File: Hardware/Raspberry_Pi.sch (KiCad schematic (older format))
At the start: 4 parts, among them J1 M20-9762042

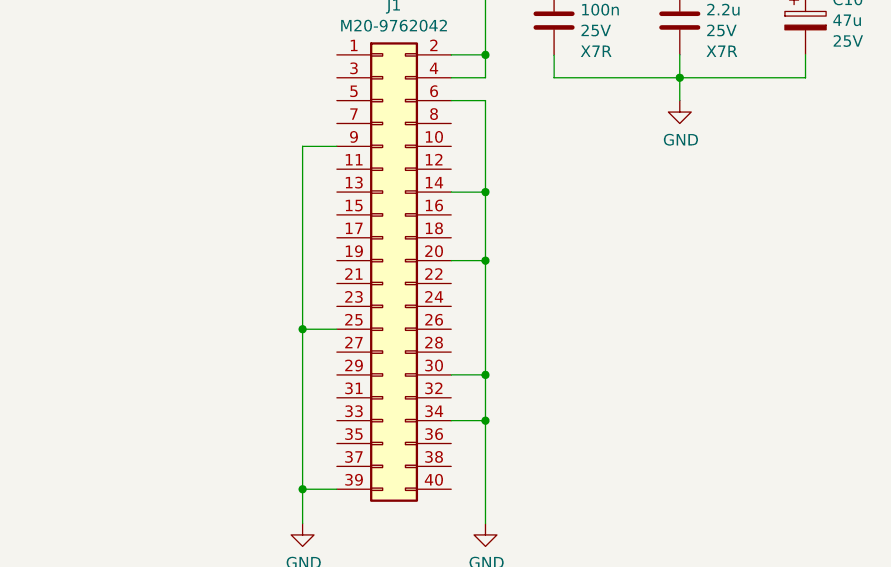
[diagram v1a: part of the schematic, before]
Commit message: [Hardware] Connected ADC to Raspberry Pi through SPI bus.
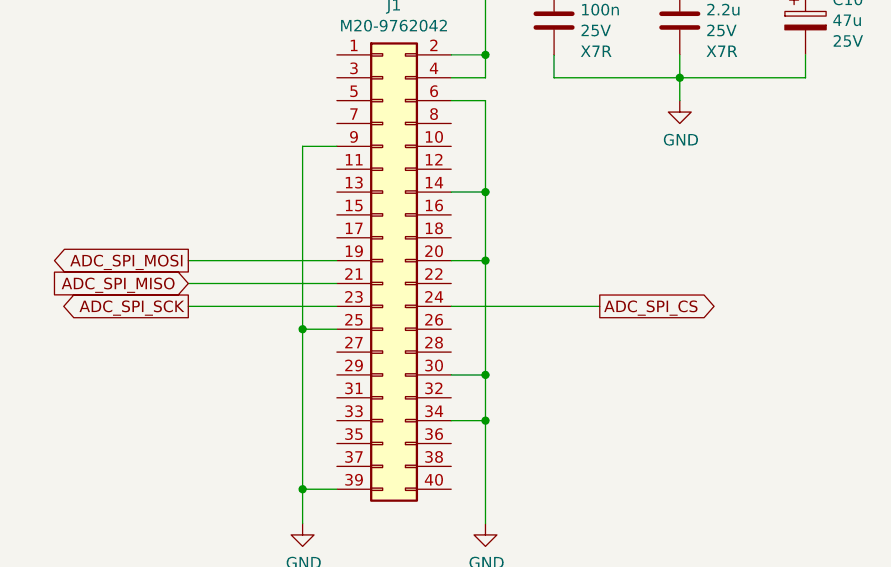
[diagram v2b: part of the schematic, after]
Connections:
- net ADC_SPI_MOSI: now reaches J1.19 (Pin_19)
- net ADC_SPI_MISO: now reaches J1.21 (Pin_21)
- net ADC_SPI_SCK: now reaches J1.23 (Pin_23)
- net ADC_SPI_CS: now reaches J1.24 (Pin_24)
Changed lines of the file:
@@
 Wire Wire Line
 	5050 3950 5050 4100
+Wire Wire Line
+	5200 3150 4550 3150
+Text GLabel 4550 3150 0    50   Output ~ 0
+ADC_SPI_SCK
+Wire Wire Line
+	5200 3050 4550 3050
+Text GLabel 4550 3050 0    50   Input ~ 0
+ADC_SPI_MISO
+Text GLabel 4550 2950 0    50   Output ~ 0
+ADC_SPI_MOSI
+Wire Wire Line
+	5200 2950 4550 2950
+Wire Wire Line
+	6350 3150 5700 3150
+Text GLabel 6350 3150 2    50   Output ~ 0
+ADC_SPI_CS
 $EndSCHEMATC

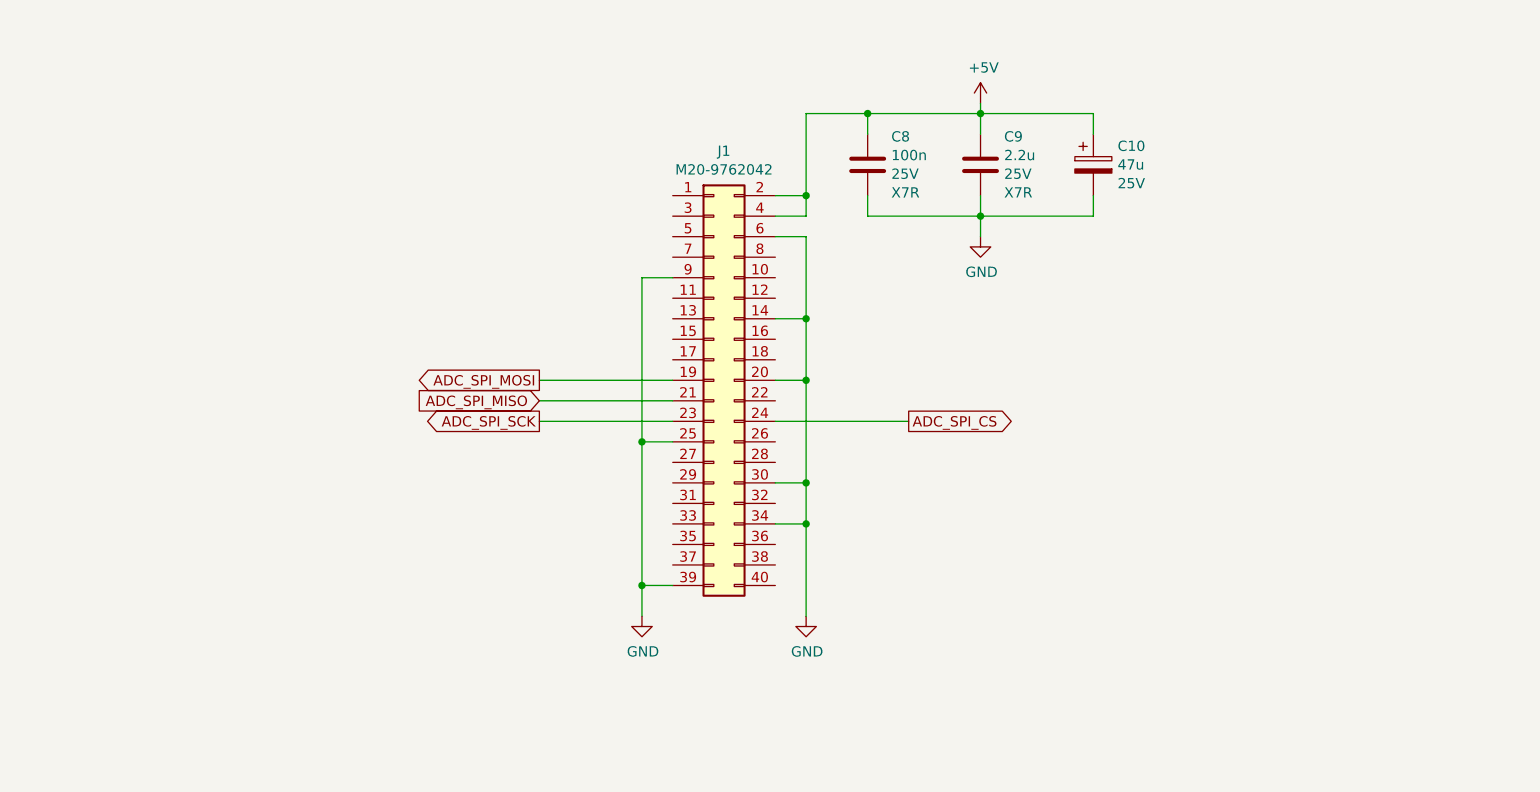
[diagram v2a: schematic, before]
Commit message: [Hardware] Added servomotors supply parts and connected them to Raspberry Pi PWMs.
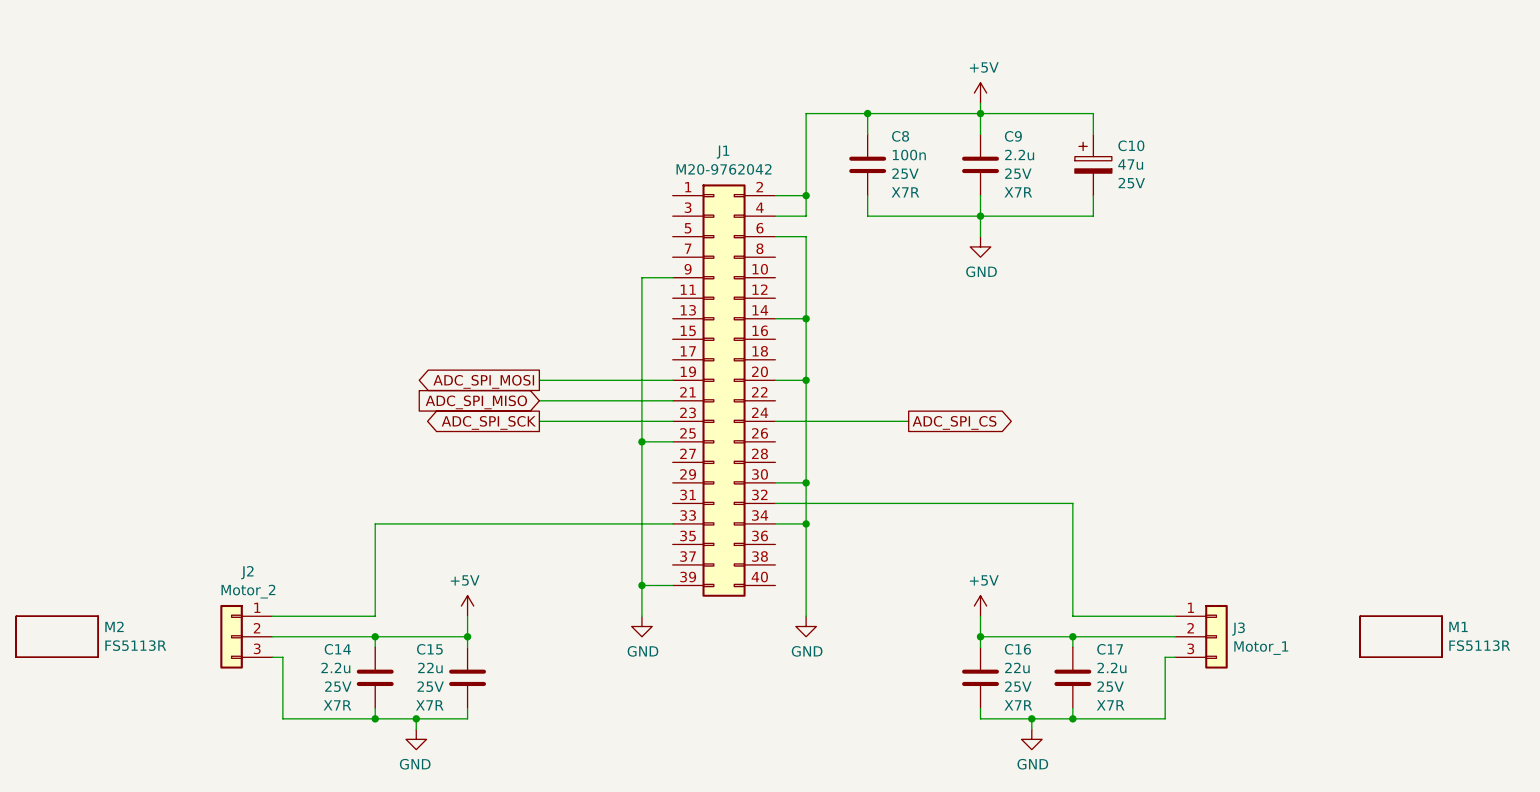
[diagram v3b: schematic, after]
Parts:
- added C14, C17: 2.2u, Capacitor_SMD:C_1206_3216Metric_Pad1.42x1.75mm_HandSolder, symbol Device:C
- added C15, C16: 22u, Capacitor_SMD:C_1206_3216Metric_Pad1.42x1.75mm_HandSolder, symbol Device:C
- added J2: Motor_2, Connector_PinHeader_2.54mm:PinHeader_1x03_P2.54mm_Vertical, symbol Connector_Generic:Conn_01x03
- added J3: Motor_1, Connector_PinHeader_2.54mm:PinHeader_1x03_P2.54mm_Vertical, symbol Connector_Generic:Conn_01x03
- added M1, M2: FS5113R, Supply_Part:Supply_Part, symbol Supply_Part:Supply_Part
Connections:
- net +5V: now also C14.2, C15.2, C16.2, C17.2, J2.2 (Pin_2), J3.2 (Pin_2)
- net GND: now also C14.1, C15.1, C16.1, C17.1, J2.3 (Pin_3), J3.3 (Pin_3)
- net at J1.32 (Pin_32): now also J3.1 (Pin_1)
- net at J1.33 (Pin_33): now also J2.1 (Pin_1)
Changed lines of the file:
@@
 Text GLabel 6350 3150 2    50   Output ~ 0
 ADC_SPI_CS
+$Comp
+L Supply_Part:Supply_Part M1
+U 1 1 5F220D82
+P 8750 4200
+F 0 "M1" H 8978 4246 50  0000 L CNN
+F 1 "FS5113R" H 8978 4155 50  0000 L CNN
+F 2 "Supply_Part:Supply_Part" H 8750 4200 50  0001 C CNN
+F 3 "" H 8750 4200 50  0001 C CNN
+F 4 "Feetech" H 8750 4200 50  0001 C CNN "Value2"
+	1    8750 4200
+	1    0    0    -1
+$EndComp
+$Comp
+L Supply_Part:Supply_Part M2
+U 1 1 5F222375
+P 2200 4200
+F 0 "M2" H 2428 4246 50  0000 L CNN
+F 1 "FS5113R" H 2428 4155 50  0000 L CNN
+F 2 "Supply_Part:Supply_Part" H 2200 4200 50  0001 C CNN
+F 3 "" H 2200 4200 50  0001 C CNN
+F 4 "Feetech" H 2200 4200 50  0001 C CNN "Value2"
+	1    2200 4200
+	1    0    0    -1
+$EndComp
+$Comp
+L power:GND #PWR017
+U 1 1 5F22F17E
+P 6950 4650
+F 0 "#PWR017" H 6950 4400 50  0001 C CNN
+F 1 "GND" H 6955 4477 50  0000 C CNN
+F 2 "" H 6950 4650 50  0001 C CNN
+F 3 "" H 6950 4650 50  0001 C CNN
+	1    6950 4650
+	1    0    0    -1
+$EndComp
+$Comp
+L Connector_Generic:Conn_01x03 J3
+U 1 1 5F220658
+P 7850 4200
+F 0 "J3" H 7930 4242 50  0000 L CNN
+F 1 "Motor_1" H 7930 4151 50  0000 L CNN
+F 2 "Connector_PinHeader_2.54mm:PinHeader_1x03_P2.54mm_Vertical" H 7850 4200 50  0001 C CNN
+F 3 "~" H 7850 4200 50  0001 C CNN
+	1    7850 4200
+	1    0    0    -1
+$EndComp
+$Comp
+L Device:C C?
+U 1 1 5F23B1E7
+P 7150 4400
+AR Path="/5F1F2F9E/5F23B1E7" Ref="C?"  Part="1"
+AR Path="/5F22814A/5F23B1E7" Ref="C17"  Part="1"
+F 0 "C17" H 7035 4263 50  0000 R CNN
+F 1 "2.2u" H 7035 4354 50  0000 R CNN
+F 2 "Capacitor_SMD:C_1206_3216Metric_Pad1.42x1.75mm_HandSolder" H 7188 4250 50  0001 C CNN
+F 3 "~" H 7150 4400 50  0001 C CNN
+F 4 "25V" H 7035 4445 50  0000 R CNN "Value2"
+F 5 "X7R" H 7035 4536 50  0000 R CNN "Value3"
+	1    7150 4400
+	-1   0    0    1
+$EndComp
+$Comp
+L Device:C C?
+U 1 1 5F23F5D8
+P 6700 4400
+AR Path="/5F1F2F9E/5F23F5D8" Ref="C?"  Part="1"
+AR Path="/5F22814A/5F23F5D8" Ref="C16"  Part="1"
+F 0 "C16" H 6585 4263 50  0000 R CNN
+F 1 "22u" H 6585 4354 50  0000 R CNN
+F 2 "Capacitor_SMD:C_1206_3216Metric_Pad1.42x1.75mm_HandSolder" H 6738 4250 50  0001 C CNN
+F 3 "~" H 6700 4400 50  0001 C CNN
+F 4 "25V" H 6585 4445 50  0000 R CNN "Value2"
+F 5 "X7R" H 6585 4536 50  0000 R CNN "Value3"
+F 6 "CC1206KRX7R9BB104" V 6700 4400 50  0001 C CNN "ManufacturerReference"
+	1    6700 4400
+	-1   0    0    1
+$EndComp
+Wire Wire Line
+	6700 4550 6700 4600
+Wire Wire Line
+	6700 4600 6950 4600
+Wire Wire Line
+	6950 4600 6950 4650
+Wire Wire Line
+	6950 4600 7150 4600
+Wire Wire Line
+	7150 4600 7150 4550
+Connection ~ 6950 4600
+Wire Wire Line
+	7150 4600 7600 4600
+Wire Wire Line
+	7600 4600 7600 4300
+Wire Wire Line
+	7600 4300 7650 4300
+Connection ~ 7150 4600
+Wire Wire Line
+	6700 4200 6700 4250
+Wire Wire Line
+	6700 4200 7150 4200
+Wire Wire Line
+	7150 4200 7150 4250
+Wire Wire Line
+	7150 4200 7650 4200
+Connection ~ 7150 4200
+Wire Wire Line
+	5700 3550 7150 3550
+Wire Wire Line
+	7150 3550 7150 4100
+Wire Wire Line
+	7150 4100 7650 4100
+$Comp
+L power:+5V #PWR015
+U 1 1 5F24A8C3
+P 6700 4100
+F 0 "#PWR015" H 6700 3950 50  0001 C CNN
+F 1 "+5V" H 6715 4273 50  0000 C CNN
+F 2 "" H 6700 4100 50  0001 C CNN
+F 3 "" H 6700 4100 50  0001 C CNN
+	1    6700 4100
+	1    0    0    -1
+$EndComp
+Wire Wire Line
+	6700 4100 6700 4200
+Connection ~ 6700 4200
+$Comp
+L power:GND #PWR016
+U 1 1 5F250DF5
+P 3950 4650
+F 0 "#PWR016" H 3950 4400 50  0001 C CNN
+F 1 "GND" H 3955 4477 50  0000 C CNN
+F 2 "" H 3950 4650 50  0001 C CNN
+F 3 "" H 3950 4650 50  0001 C CNN
+	1    3950 4650
+	-1   0    0    -1
+$EndComp
+$Comp
+L Connector_Generic:Conn_01x03 J2
+U 1 1 5F250DFB
+P 3050 4200
+F 0 "J2" H 2968 4517 50  0000 C CNN
+F 1 "Motor_2" H 2968 4426 50  0000 C CNN
+F 2 "Connector_PinHeader_2.54mm:PinHeader_1x03_P2.54mm_Vertical" H 3050 4200 50  0001 C CNN
+F 3 "~" H 3050 4200 50  0001 C CNN
+	1    3050 4200
+	-1   0    0    -1
+$EndComp
+$Comp
+L Device:C C?
+U 1 1 5F250E03
+P 3750 4400
+AR Path="/5F1F2F9E/5F250E03" Ref="C?"  Part="1"
+AR Path="/5F22814A/5F250E03" Ref="C14"  Part="1"
+F 0 "C14" H 3635 4263 50  0000 R CNN
+F 1 "2.2u" H 3635 4354 50  0000 R CNN
+F 2 "Capacitor_SMD:C_1206_3216Metric_Pad1.42x1.75mm_HandSolder" H 3788 4250 50  0001 C CNN
+F 3 "~" H 3750 4400 50  0001 C CNN
+F 4 "25V" H 3635 4445 50  0000 R CNN "Value2"
+F 5 "X7R" H 3635 4536 50  0000 R CNN "Value3"
+	1    3750 4400
+	1    0    0    1
+$EndComp
+$Comp
+L Device:C C?
+U 1 1 5F250E0C
+P 4200 4400
+AR Path="/5F1F2F9E/5F250E0C" Ref="C?"  Part="1"
+AR Path="/5F22814A/5F250E0C" Ref="C15"  Part="1"
+F 0 "C15" H 4085 4263 50  0000 R CNN
+F 1 "22u" H 4085 4354 50  0000 R CNN
+F 2 "Capacitor_SMD:C_1206_3216Metric_Pad1.42x1.75mm_HandSolder" H 4238 4250 50  0001 C CNN
+F 3 "~" H 4200 4400 50  0001 C CNN
+F 4 "25V" H 4085 4445 50  0000 R CNN "Value2"
+F 5 "X7R" H 4085 4536 50  0000 R CNN "Value3"
+F 6 "CC1206KRX7R9BB104" V 4200 4400 50  0001 C CNN "ManufacturerReference"
+	1    4200 4400
+	1    0    0    1
+$EndComp
+Wire Wire Line
+	4200 4550 4200 4600
+Wire Wire Line
+	4200 4600 3950 4600
+Wire Wire Line
+	3950 4600 3950 4650
+Wire Wire Line
+	3950 4600 3750 4600
+Wire Wire Line
+	3750 4600 3750 4550
+Connection ~ 3950 4600
+Wire Wire Line
+	3750 4600 3300 4600
+Wire Wire Line
+	3300 4600 3300 4300
+Wire Wire Line
+	3300 4300 3250 4300
+Connection ~ 3750 4600
+Wire Wire Line
+	4200 4200 4200 4250
+Wire Wire Line
+	4200 4200 3750 4200
+Wire Wire Line
+	3750 4200 3750 4250
+Wire Wire Line
+	3750 4200 3250 4200
+Connection ~ 3750 4200
+Wire Wire Line
+	3750 4100 3250 4100
+$Comp
+L power:+5V #PWR014
+U 1 1 5F250E23
+P 4200 4100
+F 0 "#PWR014" H 4200 3950 50  0001 C CNN
+F 1 "+5V" H 4215 4273 50  0000 C CNN
+F 2 "" H 4200 4100 50  0001 C CNN
+F 3 "" H 4200 4100 50  0001 C CNN
+	1    4200 4100
+	-1   0    0    -1
+$EndComp
+Wire Wire Line
+	4200 4100 4200 4200
+Connection ~ 4200 4200
+Wire Wire Line
+	3750 3650 5200 3650
+Wire Wire Line
+	3750 3650 3750 4100
 $EndSCHEMATC

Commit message: [Hardware] Moved servomotors supply parts to main page. Also added servomotors wheels and supports supplies.
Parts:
- removed M1, M2: FS5113R, Supply_Part:Supply_Part, symbol Supply_Part:Supply_Part
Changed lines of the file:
@@
 ADC_SPI_CS
-$Comp
-L Supply_Part:Supply_Part M1
-U 1 1 5F220D82
-P 8750 4200
-F 0 "M1" H 8978 4246 50  0000 L CNN
-F 1 "FS5113R" H 8978 4155 50  0000 L CNN
-F 2 "Supply_Part:Supply_Part" H 8750 4200 50  0001 C CNN
-F 3 "" H 8750 4200 50  0001 C CNN
-F 4 "Feetech" H 8750 4200 50  0001 C CNN "Value2"
-	1    8750 4200
-	1    0    0    -1
-$EndComp
-$Comp
-L Supply_Part:Supply_Part M2
-U 1 1 5F222375
-P 2200 4200
-F 0 "M2" H 2428 4246 50  0000 L CNN
-F 1 "FS5113R" H 2428 4155 50  0000 L CNN
-F 2 "Supply_Part:Supply_Part" H 2200 4200 50  0001 C CNN
-F 3 "" H 2200 4200 50  0001 C CNN
-F 4 "Feetech" H 2200 4200 50  0001 C CNN "Value2"
-	1    2200 4200
-	1    0    0    -1
-$EndComp
 $Comp
 L power:GND #PWR017

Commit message: [Hardware] Added a transistor to enable leds control from Raspberry Pi.
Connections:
- net CAMERA_BOARD_LEDS: now reaches J1.18 (Pin_18)
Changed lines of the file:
@@
 Wire Wire Line
 	3750 3650 3750 4100
+Wire Wire Line
+	6350 2850 5700 2850
+Text GLabel 6350 2850 2    50   Output ~ 0
+CAMERA_BOARD_LEDS
 $EndSCHEMATC

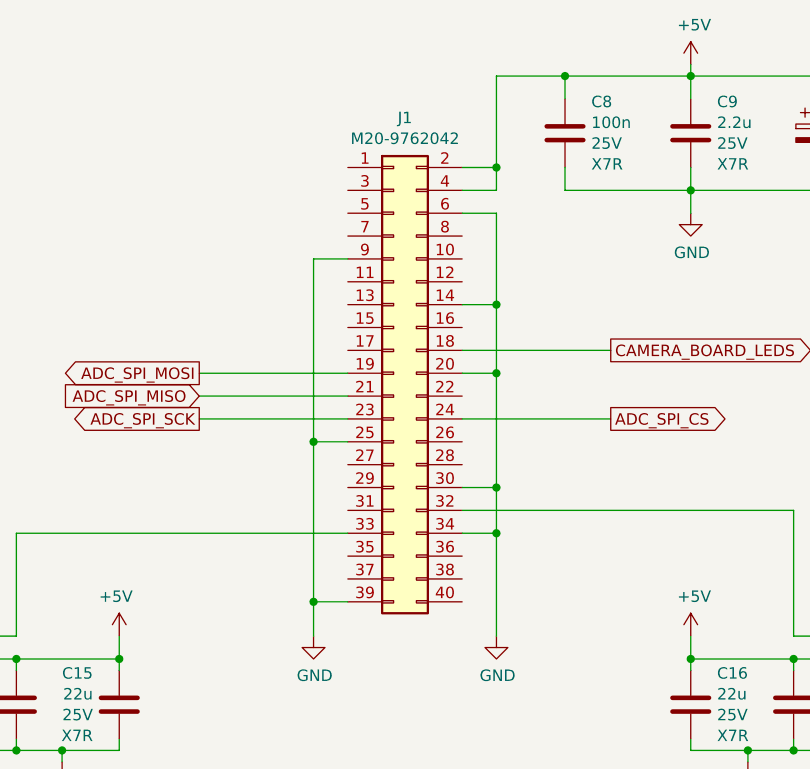
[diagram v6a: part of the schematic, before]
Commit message: [Hardware] Added IHLP3232DZER3R3M01 inductor footprint.
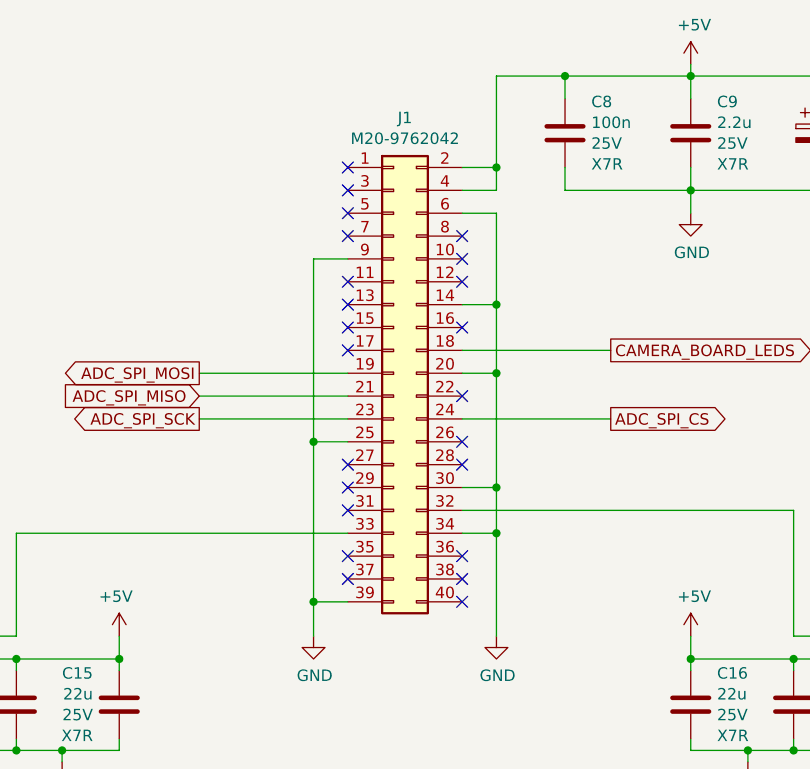
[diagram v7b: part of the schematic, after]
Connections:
- no-connect marks 0 -> 23
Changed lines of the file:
@@
 Text GLabel 6350 2850 2    50   Output ~ 0
 CAMERA_BOARD_LEDS
+NoConn ~ 5200 2050
+NoConn ~ 5200 2150
+NoConn ~ 5200 2250
+NoConn ~ 5200 2350
+NoConn ~ 5700 2350
+NoConn ~ 5700 2450
+NoConn ~ 5700 2550
+NoConn ~ 5200 2550
+NoConn ~ 5200 2650
+NoConn ~ 5200 2750
+NoConn ~ 5200 2850
+NoConn ~ 5700 2750
+NoConn ~ 5700 3050
+NoConn ~ 5700 3250
+NoConn ~ 5700 3350
+NoConn ~ 5200 3350
+NoConn ~ 5200 3450
+NoConn ~ 5200 3550
+NoConn ~ 5200 3750
+NoConn ~ 5200 3850
+NoConn ~ 5700 3750
+NoConn ~ 5700 3850
+NoConn ~ 5700 3950
 $EndSCHEMATC
